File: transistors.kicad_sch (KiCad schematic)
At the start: 22 parts, among them J11 Transistor_2, J12 Transistor_1, J13 Transistor_4, J14 Transistor_.3, Q1 DMN2011UTS, Q2 DMN2011UTS, Q3 DMN2011UTS, Q4 DMN2011UTS

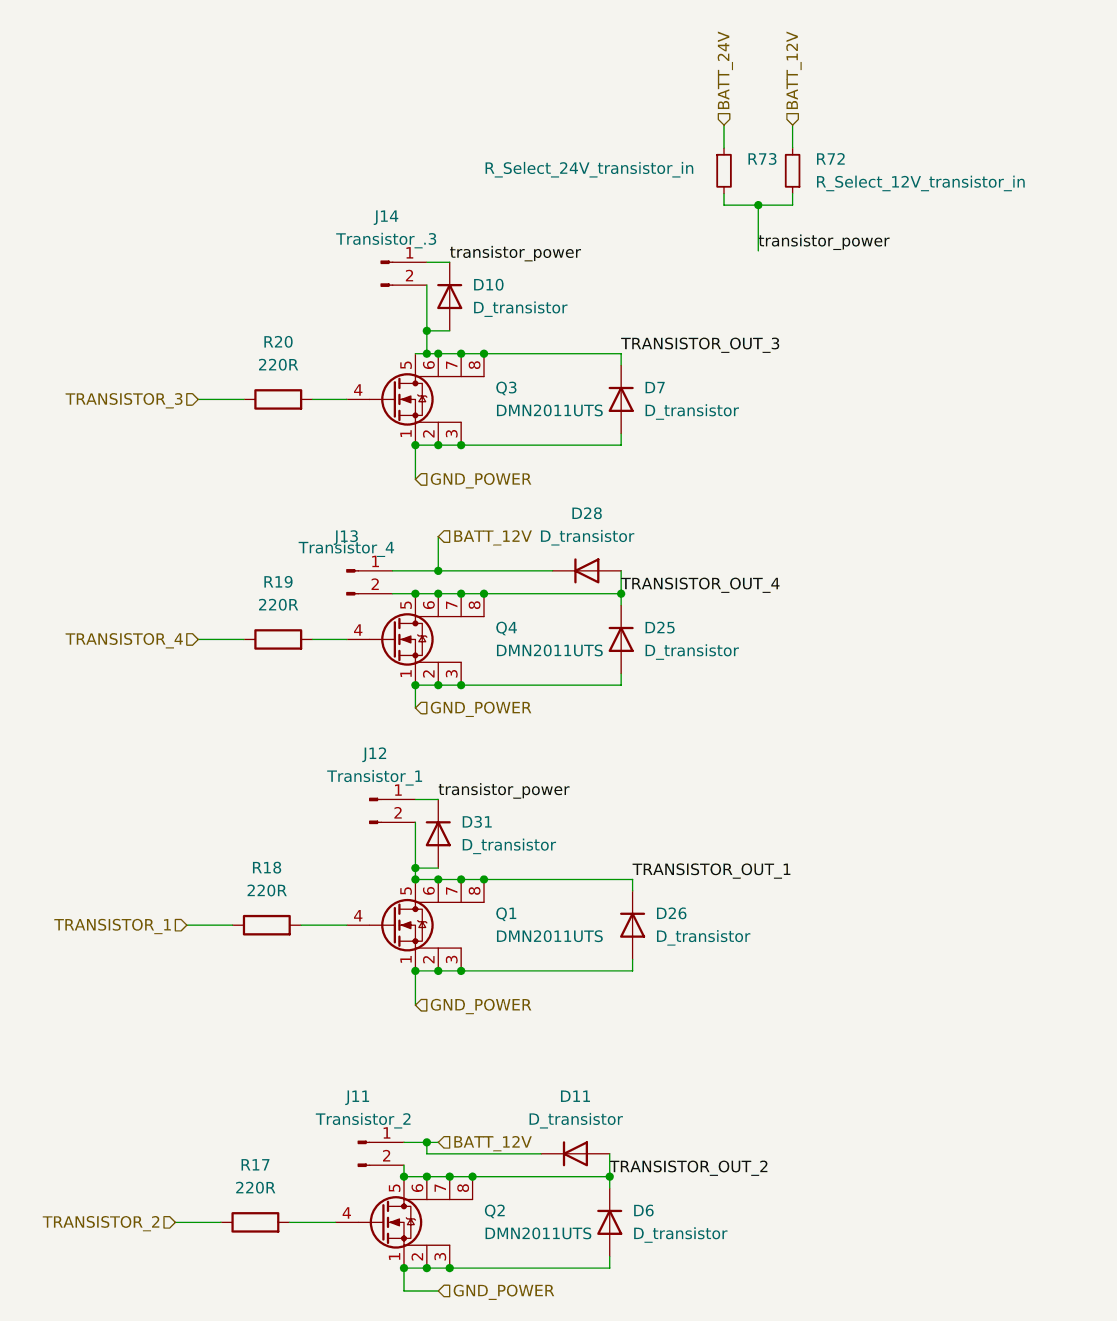
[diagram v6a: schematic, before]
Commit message: fix diodes on transistors + fix warnings
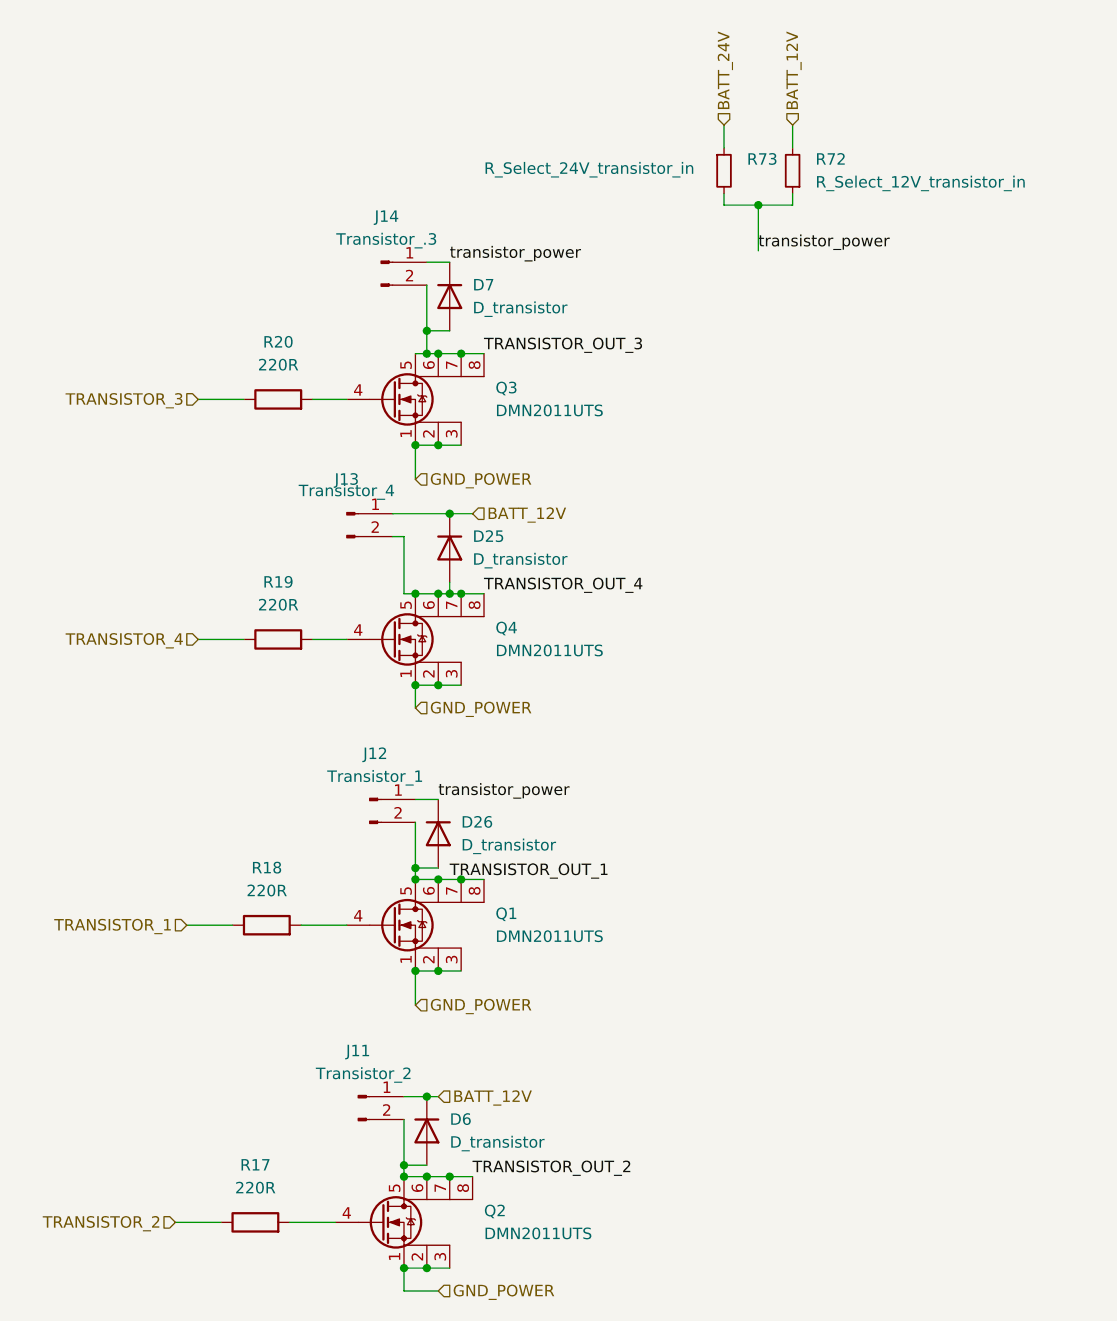
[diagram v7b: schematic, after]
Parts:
- removed D10, D11, D28, D31: D_transistor, Diode_SMD:D_SOD-123, symbol Device:D
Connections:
- net BATT_12V: now also D25.1 (K), D6.1 (K)
- net GND_POWER: no longer D25.2 (A), D26.2 (A), D6.2 (A), D7.2 (A)
- net TRANSISTOR_OUT_1: now also D26.2 (A); no longer D26.1 (K)
- net TRANSISTOR_OUT_2: now also D6.2 (A); no longer D6.1 (K)
- net TRANSISTOR_OUT_3: now also D7.2 (A); no longer D7.1 (K)
- net TRANSISTOR_OUT_4: now also D25.2 (A); no longer D25.1 (K)
- net transistor_power: now also D26.1 (K), D7.1 (K)
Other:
- moved on the sheet: J11, J13
